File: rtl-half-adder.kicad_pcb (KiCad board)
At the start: 2 copper layers, 152.4 x 114.3 mm, 81 parts, among them Q1 Q_NPN_EBC, Q10 Q_NPN_EBC, Q11 Q_NPN_EBC, Q12 Q_NPN_EBC, Q13 Q_NPN_EBC, Q14 Q_NPN_EBC, Q15 Q_NPN_EBC, Q16 Q_NPN_BEC, Q17 Q_NPN_BEC, Q18 Q_NPN_BEC, Q19 Q_NPN_BEC, Q2 Q_NPN_EBC, Q3 Q_NPN_EBC, Q4 Q_NPN_EBC, Q5 Q_NPN_EBC, Q6 Q_NPN_EBC, Q7 Q_NPN_EBC, Q8 Q_NPN_EBC, Q9 Q_NPN_EBC, SW1 SW_SPDT, SW2 SW_SPDT, SW3 SW_SPDT

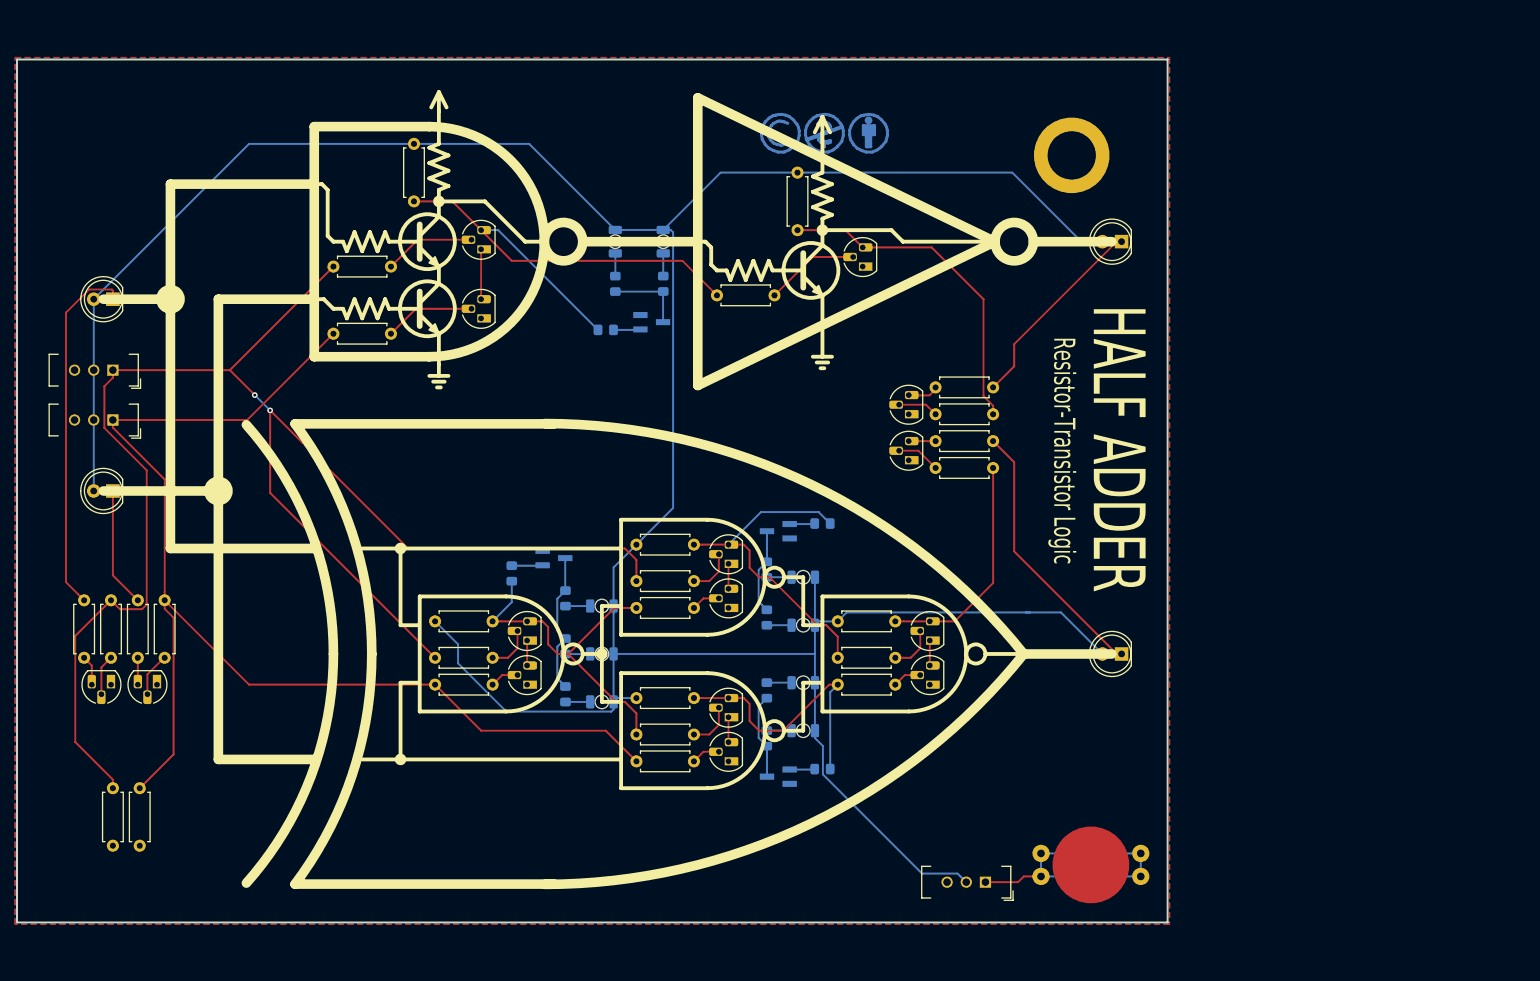
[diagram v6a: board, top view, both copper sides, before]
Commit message: full smd led array layout done
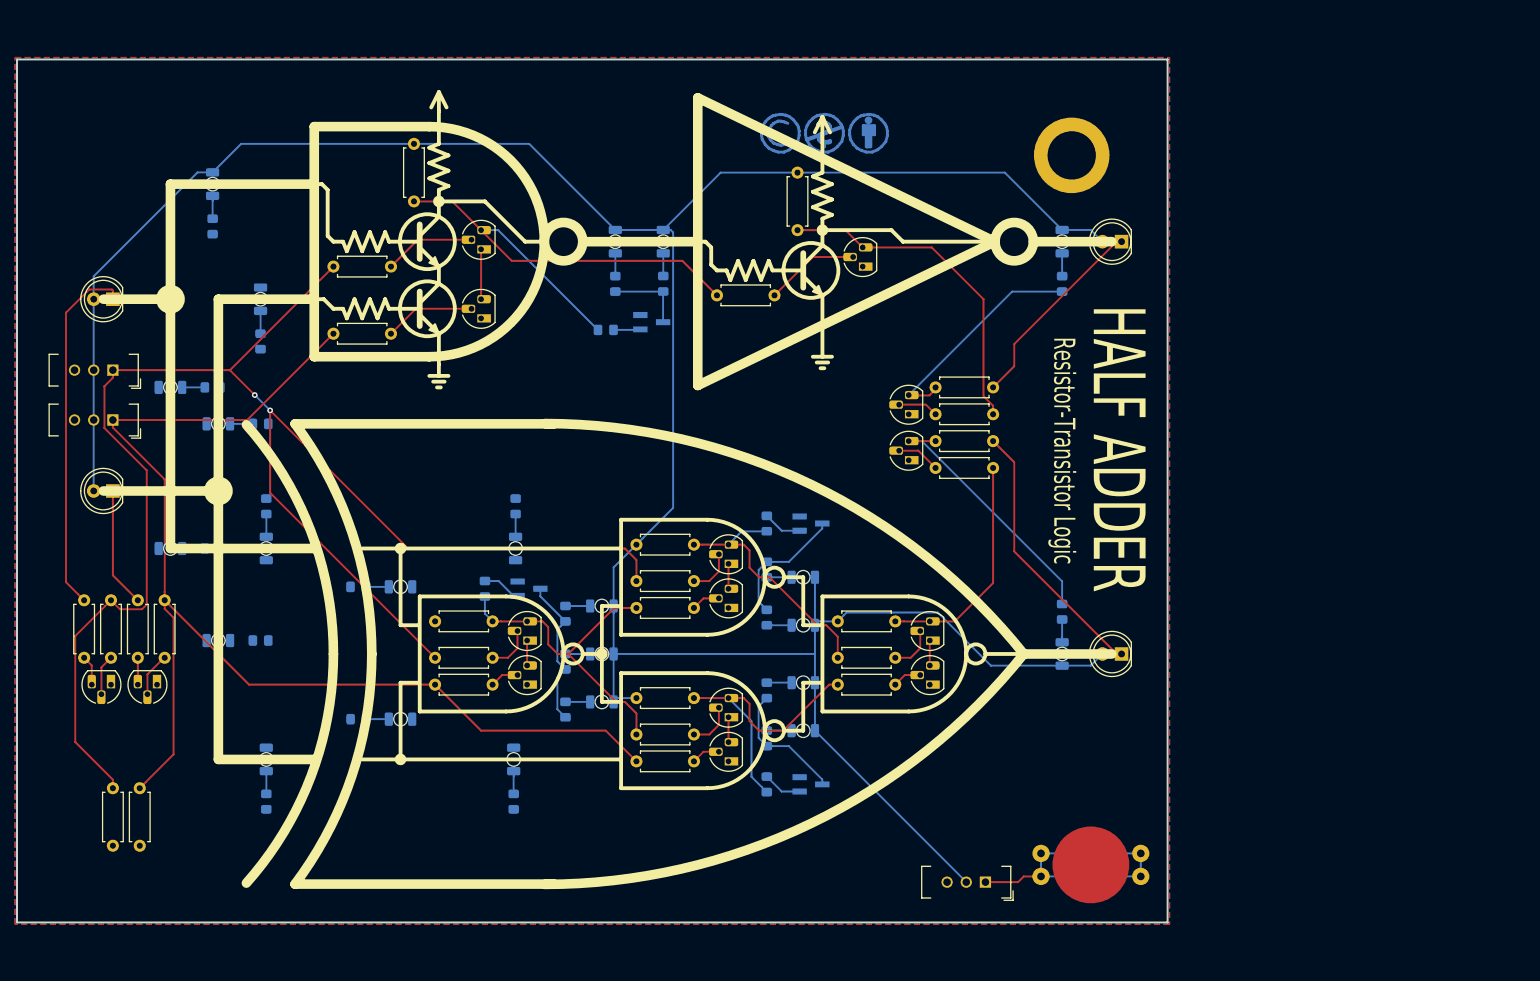
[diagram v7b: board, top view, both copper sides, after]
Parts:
- added D14: LED, --Project:LED_1206_3216Metric_ReverseMount_Hole1.8x2.4mm, B.Cu at (76.7, 54.6)
- added D15: LED, --Project:LED_1206_3216Metric_ReverseMount_Hole1.8x2.4mm, B.Cu at (71.1, 81.5)
- added D16: LED, --Project:LED_1206_3216Metric_ReverseMount_Hole1.8x2.4mm, B.Cu at (71.1, 102.9)
- added D17: LED, --Project:LED_1206_3216Metric_ReverseMount_Hole1.8x2.4mm, B.Cu at (83.8, 102.9)
- added D18: LED, --Project:LED_1206_3216Metric_ReverseMount_Hole1.8x2.4mm, B.Cu at (101.6, 108.0)
- added D19: LED, --Project:LED_1206_3216Metric_ReverseMount_Hole1.8x2.4mm, B.Cu at (116.8, 102.9)
- added D20: LED, --Project:LED_1206_3216Metric_ReverseMount_Hole1.8x2.4mm, B.Cu at (83.1, 69.8)
- added D21: LED, --Project:LED_1206_3216Metric_ReverseMount_Hole1.8x2.4mm, B.Cu at (77.5, 86.4)
- added D22: LED, --Project:LED_1206_3216Metric_ReverseMount_Hole1.8x2.4mm, B.Cu at (77.5, 115.1)
- added D23: LED, --Project:LED_1206_3216Metric_ReverseMount_Hole1.8x2.4mm, B.Cu at (83.8, 130.8)
- added D24: LED, --Project:LED_1206_3216Metric_ReverseMount_Hole1.8x2.4mm, B.Cu at (101.6, 125.5)
- added D25: LED, --Project:LED_1206_3216Metric_ReverseMount_Hole1.8x2.4mm, B.Cu at (116.6, 130.8)
- added D26: LED, --Project:LED_1206_3216Metric_ReverseMount_Hole1.8x2.4mm, B.Cu at (189.2, 62.2)
- added D27: LED, --Project:LED_1206_3216Metric_ReverseMount_Hole1.8x2.4mm, B.Cu at (189.2, 116.8)
- added R41: 68, Resistor_SMD:R_0805_2012Metric_Pad1.15x1.40mm_HandSolder, B.Cu at (76.7, 60.2)
- added R42: 68, Resistor_SMD:R_0805_2012Metric_Pad1.15x1.40mm_HandSolder, B.Cu at (76.7, 81.5)
- added R43: 68, Resistor_SMD:R_0805_2012Metric_Pad1.15x1.40mm_HandSolder, B.Cu at (76.7, 102.9)
- added R44: 68, Resistor_SMD:R_0805_2012Metric_Pad1.15x1.40mm_HandSolder, B.Cu at (83.8, 97.3)
- added R45: 68, Resistor_SMD:R_0805_2012Metric_Pad1.15x1.40mm_HandSolder, B.Cu at (96.0, 108.0)
- added R46: 68, Resistor_SMD:R_0805_2012Metric_Pad1.15x1.40mm_HandSolder, B.Cu at (116.8, 97.3)
- added R47: 68, Resistor_SMD:R_0805_2012Metric_Pad1.15x1.40mm_HandSolder, B.Cu at (83.1, 75.4)
- added R48: 68, Resistor_SMD:R_0805_2012Metric_Pad1.15x1.40mm_HandSolder, B.Cu at (83.1, 86.4)
- added R49: 68, Resistor_SMD:R_0805_2012Metric_Pad1.15x1.40mm_HandSolder, B.Cu at (83.1, 115.1)
- added R50: 68, Resistor_SMD:R_0805_2012Metric_Pad1.15x1.40mm_HandSolder, B.Cu at (83.8, 136.4)
- added R51: 68, Resistor_SMD:R_0805_2012Metric_Pad1.15x1.40mm_HandSolder, B.Cu at (96.0, 125.5)
- added R52: 68, Resistor_SMD:R_0805_2012Metric_Pad1.15x1.40mm_HandSolder, B.Cu at (116.6, 136.4)
- added R53: 68, Resistor_SMD:R_0805_2012Metric_Pad1.15x1.40mm_HandSolder, B.Cu at (189.2, 67.8)
- added R54: 68, Resistor_SMD:R_0805_2012Metric_Pad1.15x1.40mm_HandSolder, B.Cu at (189.2, 111.3)
- moved R38 7.64 mm to (150.1, 134.1), turned to 270 degrees
- moved R35 7.37 mm to (150.1, 99.6), turned to 270 degrees
- moved Q17 5.24 mm to (118.6, 108.2)
- moved Q18 4.44 mm to (156.0, 99.6), turned to 0 degrees
- moved Q19 4.44 mm to (156.0, 134.1), turned to 0 degrees
- moved R31 4.10 mm to (112.8, 108.2)
- moved R32 2.03 mm to (123.4, 111.5), turned to 270 degrees
- moved R33 2.03 mm to (123.4, 117.9), turned to 270 degrees
- moved R34 2.03 mm to (123.4, 124.2), turned to 270 degrees
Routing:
- net VCC: track 400.2 -> 368.8 mm
- net /SUM_GATE: track 3.56 -> 34.6 mm
- net /CARRY_GATE: track 3.90 -> 29.9 mm
- net XOR2: track 44.1 -> 34.0 mm
- net Net-(Q18-Pad3): track 11.3 -> 17.1 mm
- net Net-(Q19-Pad3): track 11.3 -> 17.1 mm
- net Net-(D14-Pad1): track 0.00 -> 3.02 mm
- net Net-(D18-Pad1): track 0.00 -> 3.02 mm
- net Net-(D27-Pad1): track 0.00 -> 3.01 mm
- net Net-(D26-Pad1): track 0.00 -> 3.01 mm
- net Net-(D21-Pad1): track 0.00 -> 3.01 mm
- net Net-(D16-Pad1): track 0.00 -> 3.01 mm
- net Net-(D15-Pad1): track 0.00 -> 3.01 mm
- net Net-(D24-Pad1): track 0.00 -> 3.01 mm
- net Net-(D20-Pad1): track 0.00 -> 3.01 mm
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
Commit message: layout all done
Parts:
- removed the REF** at (139.4, 46.0)
- added REF**: OSHW-Logo_11.4x12mm_Copper, Symbol:OSHW-Logo_11.4x12mm_Copper, B.Cu at (86.6, 143.3)
- moved REF** 107.8 mm to (118.9, 145.9)
- moved REF** 107.8 mm to (113.0, 145.9)
- moved REF** 107.8 mm to (107.2, 145.9)
- moved R44 10.2 mm to (84.8, 107.4), turned to 0 degrees
- moved R46 10.2 mm to (115.8, 107.4), turned to 180 degrees
- moved R50 10.2 mm to (84.8, 126.2), turned to 0 degrees
- moved R52 10.2 mm to (115.6, 126.2), turned to 180 degrees
- moved Q17 8.64 mm to (126.5, 104.6)
- moved R31 8.64 mm to (120.7, 104.6)
- moved D18 0.25 mm to (101.6, 108.2)
- moved R45 0.25 mm to (96.0, 108.2)
- turned D17 to 90 degrees
- turned D19 to 90 degrees
- turned D23 to 270 degrees
- turned D25 to 270 degrees
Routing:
- net VCC: track 368.8 -> 692.2 mm
- net /B_GATE: track 3.43 -> 141.3 mm
- net /A_GATE: track 3.85 -> 128.9 mm
- net Net-(Q17-Pad3): track 20.2 -> 25.8 mm
- net XOR1: track 43.5 -> 47.6 mm
- net Net-(D22-Pad1): track 0.00 -> 3.01 mm
- net A: track 212.0 -> 210.4 mm
